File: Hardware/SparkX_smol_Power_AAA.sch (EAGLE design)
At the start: 35 parts, among them J3 AVR_SPI_PROG_3X2TESTPOINTS, U1 ATTINY43_QFN20, U2 TPS61200

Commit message: Update smôl logo
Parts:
- added U$13, U$14: SMOL_LOGOSMALL, SparkX:SMOL_LOGOSMALL
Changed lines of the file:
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@@
 <part name="RXD" library="SparkFun-Connectors" deviceset="TEST-POINT" device="3X4" value="TEST-POINT3X4"/>
 <part name="TXD" library="SparkFun-Connectors" deviceset="TEST-POINT" device="3X4" value="TEST-POINT3X4"/>
+<part name="U$13" library="SparkX" deviceset="SMOL_LOGO" device="SMALL"/>
+<part name="U$14" library="SparkX" deviceset="SMOL_LOGO" device="SMALL"/>
 </parts>
 <sheets>
@@
 <attribute name="NAME" x="99.06" y="104.14" size="1.778" layer="95" font="vector"/>
 </instance>
+<instance part="U$13" gate="G$1" x="307.34" y="40.64" smashed="yes"/>
+<instance part="U$14" gate="G$1" x="307.34" y="40.64" smashed="yes"/>
 </instances>
 <busses>

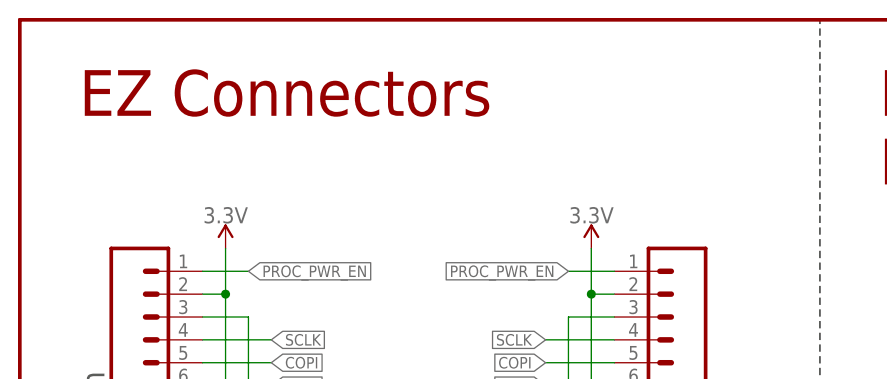
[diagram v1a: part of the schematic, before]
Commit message: Change EZ to smôl on schematic
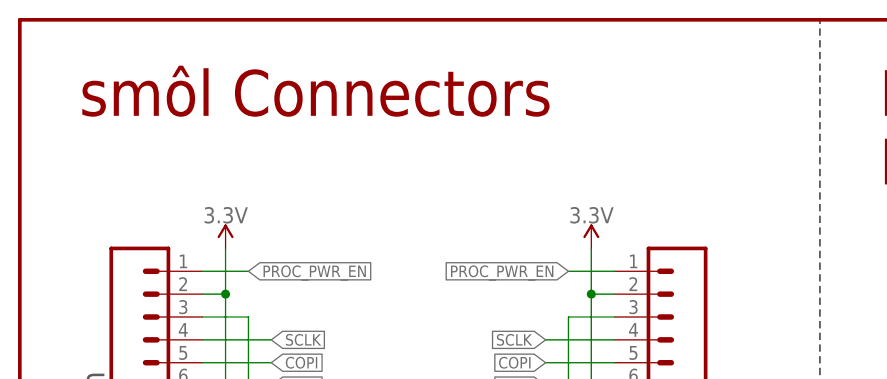
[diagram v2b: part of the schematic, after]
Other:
- note added: "smôl Connectors"
- note removed: "EZ Connectors"
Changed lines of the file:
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@@
 <wire x1="88.9" y1="190.5" x2="88.9" y2="279.4" width="0.2032" layer="97" style="longdash"/>
 <wire x1="88.9" y1="190.5" x2="0" y2="190.5" width="0.2032" layer="97" style="longdash"/>
-<text x="6.604" y="268.732" size="5.08" layer="94">EZ Connectors</text>
+<text x="6.604" y="268.732" size="5.08" layer="94">smôl Connectors</text>
 <text x="76.962" y="236.22" size="2.54" layer="97" font="vector" rot="R270">Top</text>
 <text x="9.398" y="228.854" size="2.54" layer="97" font="vector" rot="R90">Bottom</text>
